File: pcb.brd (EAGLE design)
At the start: 88.9 x 70 mm, 83 parts, among them U1.1 REG101-3_DBV_5, U2.1 TCA6416A_PW_24, U4.1 TLV2242_D_8, U6.1 DCH010505S_EDJ_4, U6.2 ISO7221A_D_8, U6.3 TS5A3357_DCU_8, U6.4 TS5A3357_DCU_8, U8.1 DCH010505S_EDJ_4, U8.2 MAX232E_D_16, U8.3 ISO7221A_D_8, U9.1 DCH010505S_EDJ_4, U9.2 ISO7420Fx

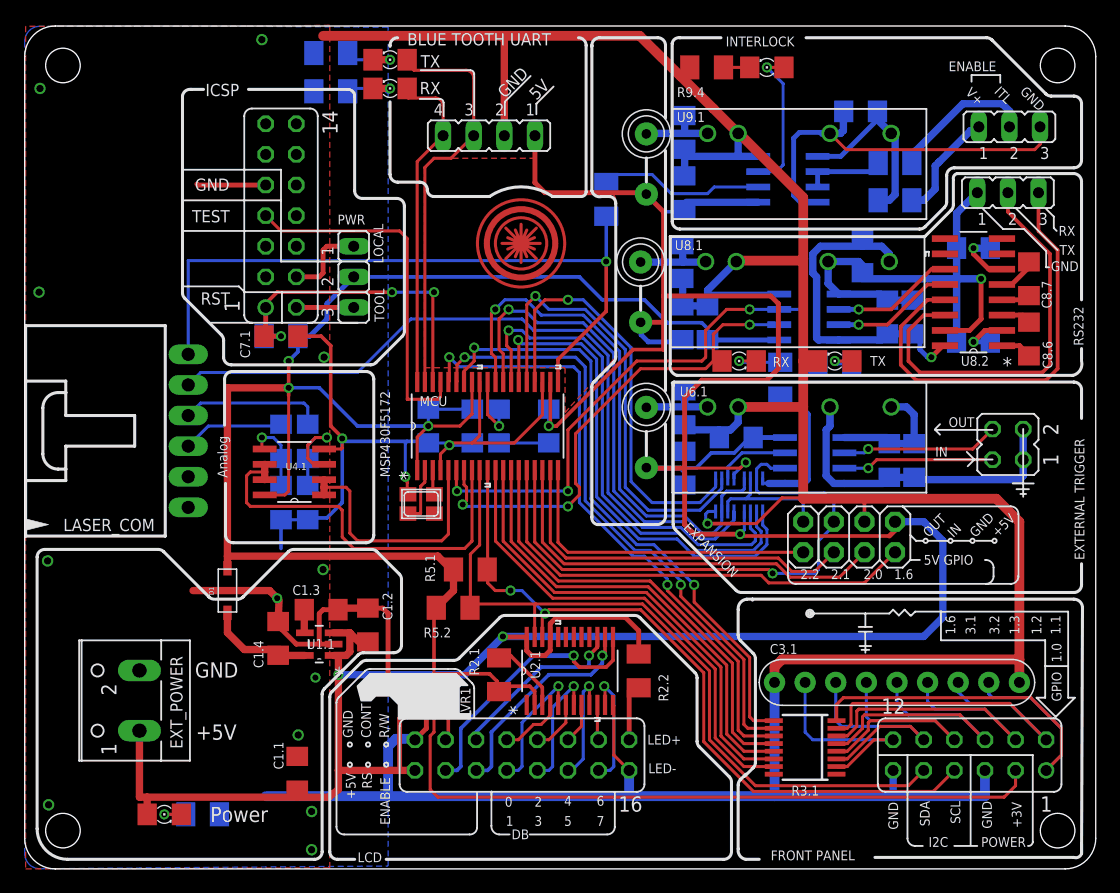
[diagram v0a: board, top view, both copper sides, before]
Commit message: Separated Analog ground from digital ground
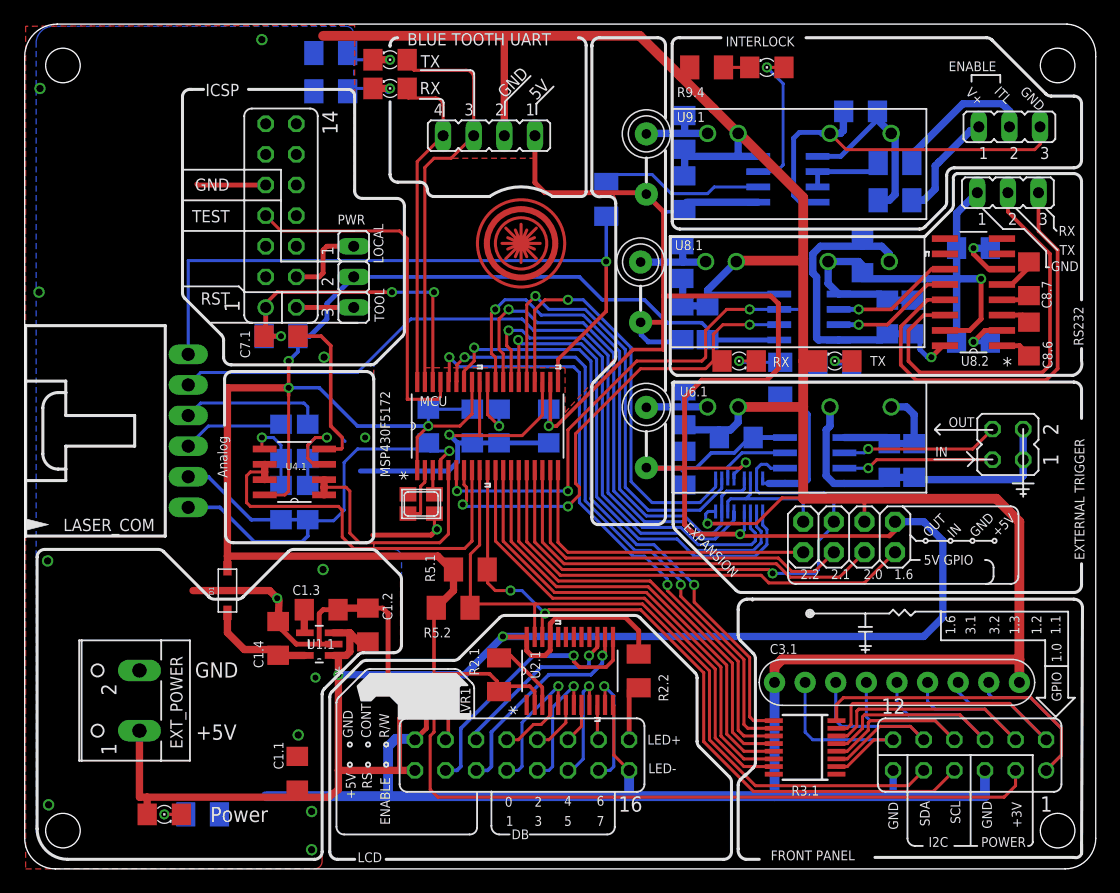
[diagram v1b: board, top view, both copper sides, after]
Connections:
- removed net G2: XTL.2
- new net A_GND: C5.1.2, LASER_COM.1, LASER_COM.2, MCU.4, R4.1.1, R4.3.1
- new net G1: XTL.4
- net GND: now also XTL.2; no longer C5.1.2, LASER_COM.1, LASER_COM.2, MCU.4, R4.1.1, R4.3.1, XTL.4
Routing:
- net A_GND: track 0.00 -> 43.1 mm, vias 0 -> 1
- net GND: track 408.3 -> 395.6 mm
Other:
- board size 88.9 x 70 mm -> 88.9 x 70.1 mm

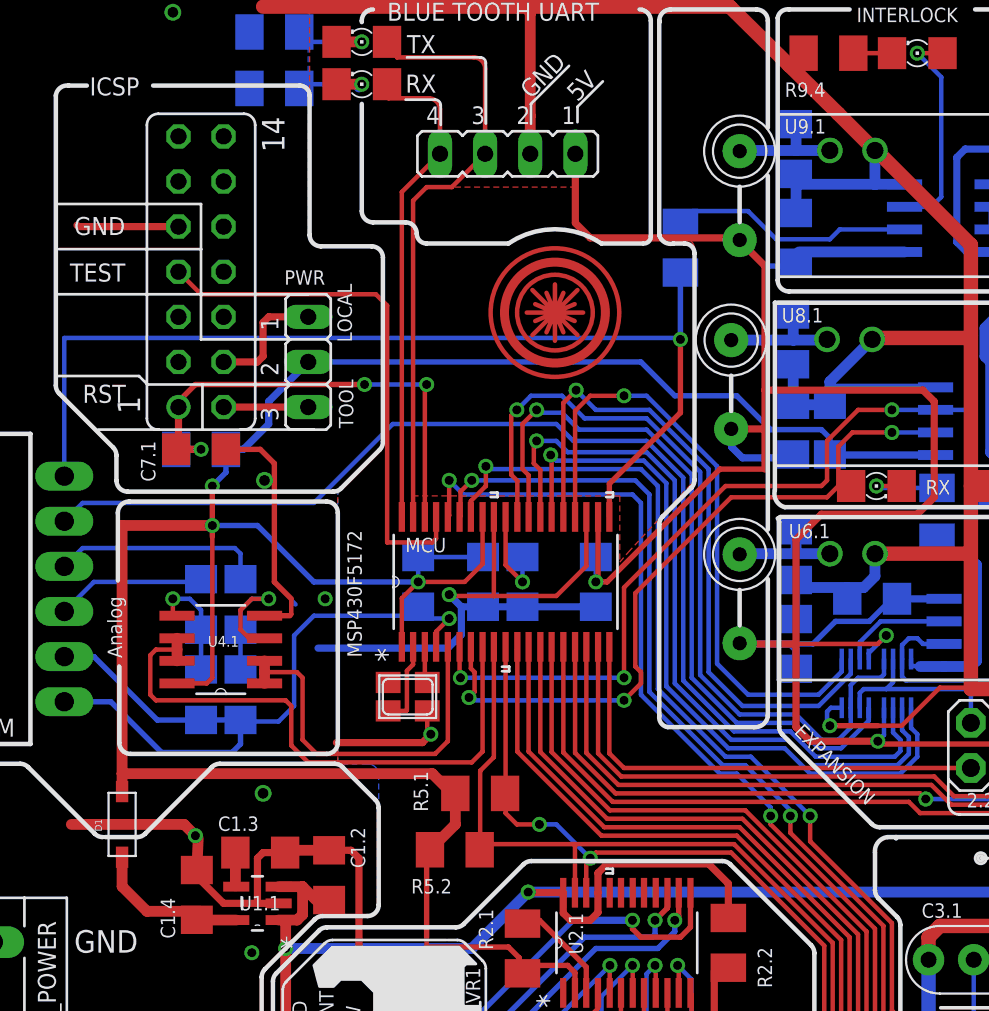
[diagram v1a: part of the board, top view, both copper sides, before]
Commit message: Analog ground isolation
Moved opamp to Agnd
added Agnd plane
Added decoupling cap to opamp
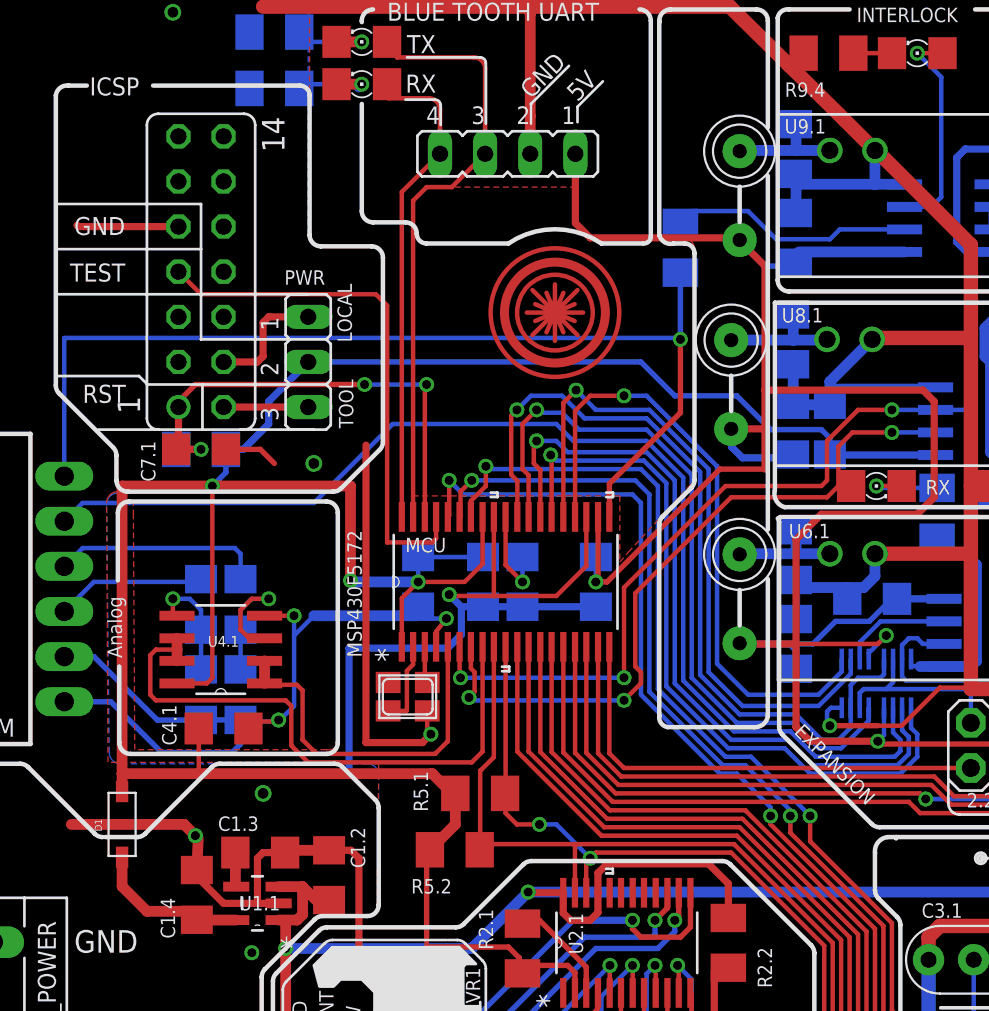
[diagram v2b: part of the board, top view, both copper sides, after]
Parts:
- added C4.1: 10 uF, adafruit:C1206
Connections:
- net A_GND: now also C4.1.1, U4.1.4
- net GND: no longer U4.1.4
- net VCC_3V: now also C4.1.2
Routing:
- net GND: track 395.6 -> 405.8 mm, vias 16 -> 15
- net VCC_3V: track 209.9 -> 218.7 mm
- net A_GND: track 43.1 -> 47.5 mm, vias 1 -> 3
- net LASER_CURRENT_3V: track 21.1 -> 22.5 mm
- net RX1: track 40.4 -> 41.1 mm
- added copper zone on layer 1, net A_GND
- added copper zone on layer 16, net A_GND

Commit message: Updated Schematic.
Updated schematic layout. Added frame, updated passive components, set
(some) resistor values.
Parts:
- removed C1.1, C4.1, C6.3, C8.4: 10 uF, adafruit:C1206
- removed C1.2, C1.4, C5.2, C5.3, C5.4, C6.4, C6.5, C8.10, C8.3, C8.9: 0.1 uF, adafruit:C1206
- removed C1.3: 0.01 uF, adafruit:C1206
- removed C6.1, C8.1, C9.1: 4.7 uF, adafruit:C1206
- removed C6.2, C8.2, C9.2, C9.3: 2.2 uF, adafruit:C1206
- removed C7.1: 2.2 nF, adafruit:C1206
- removed C8.5, C8.6, C8.7, C8.8: 1 uF, adafruit:C1206
- removed D1: (no value), adafruit:SOD-123
- removed L6.1, L8.1, L9.1: 3 uH, adafruit:FB
- removed R1.1, R7.1: 47k, adafruit:M1206
- removed R2.1: 10k, adafruit:M1206
- removed R2.2: (no value), adafruit:M1206
- removed R4.1: 1M, adafruit:R1206
- removed R4.2: 0R, adafruit:R1206
- removed R4.3: 600k, adafruit:R1206
- removed R4.4: 400k, adafruit:R1206
- removed R5.1, R5.2: 43k, adafruit:M1206
- removed R8.1, R8.2, R8.3, R8.4, R9.4: 100k, adafruit:M1206
- removed R9.2: 500k, adafruit:M1206
- removed U4.1: TLV2242_D_8, TI:D8
- added C1, C11, C12, C13, C16, C18, C2, C23, C27, C3, C6, C7, C8: .1uF, rc-master-smd:C0603
- added C10, C17, C26, C5: 10uF, rc-master-smd:C0603
- added C14, C15: 1uF, rc-master-smd:C0603
- added C19, C21, C24: 2.2uF, rc-master-smd:C0603
- added C20, C22, C25: 4.7uF, rc-master-smd:C0603
- added C4: 2.2nF, rc-master-smd:C0603
- added C9: .01uF, rc-master-smd:C0603
- added D2: BAR43, diode:SOT23
- added L1, L2, L3: 3uH, rc-master-smd:L0805
- added R1, R3: 1.2K, rc-master-smd:R0603
- added R10, R11, R12, R13, R6, R9: 330, rc-master-smd:R0603
- added R2: 47K, rc-master-smd:R0603
- added R4: 600K, rc-master-smd:R0603
- added R5: 400K, rc-master-smd:R0603
- added R7: 10K, rc-master-smd:R0603
- added R8: (no value), rc-master-smd:R0603
- added U1: TLV2242_D_8, op-amp:SO08
- C5.1: device adafruit:C1206 -> rc-master-smd:C0603
- R9.3: value 500k -> 1.2K
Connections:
- net TTL_IN_ISO renamed N$11
- removed net G1: XTL.4
- removed net ITL_POWER: C9.2.1, L9.1.P$2, U9.1.1
- removed net N$10: R4.3.2, R4.4.1, U4.1.3
- removed net N$11 (its old number): C6.2.1, L6.1.P$2, U6.1.1
- removed net N$31: LED8.2.C, R8.2.1
- removed net N$35: H9.1.1, R9.2.1
- removed net N$8 (its old number): R4.1.2, R4.2.1, U4.1.5
- removed net SERIAL_GND: C8.3.1, C8.4.1, C8.5.1, C8.8.1, C8.9.2, H8.1.1, U8.1.3, U8.2.15, U8.3.5
- removed net SERIAL_VCC: C8.3.2, C8.4.2, C8.9.1, U8.1.4, U8.2.16, U8.3.8
- removed net VCC_3V: C4.1.2, C5.1.1, C5.2.1, C8.10.1, D1.C, H3.1.3, H7.1.2, MCU.1, MCU.31, R2.1.2, R5.1.1, R5.2.1, R7.1.2, U2.1.2, U4.1.8, U8.3.1
- removed net VCC_3V_SUPPLY: C1.4.1, D1.A, U1.1.5
- new net +3V3: C1.1, C11.1, C16.2, C5.1.1, C6.2, D2.1, H3.1.3, H7.1.2, MCU.1, MCU.31, R1.1, R2.2, R3.1, R7.2, U1.1.5, U1.8, U2.1.2, U8.3.1
- new net +5V: C10.1, C20.1, C22.1, C23.2, C25.1, C27.2, C3.1, C7.1, C8.2, D2.3, EXT_POWER.1, H6.1.8, H8.2.1, L1.2, L2.2, L3.2, LED1.A, MCU.21, R8.2, U1.1.1, U1.1.3, U2.1.21, U2.1.24, U6.2.8, U6.3.8, U6.4.8, U9.2.8, VR1.3
- new net N$18: R4.1, R5.1, U1.3
- new net N$20: LED1.C, R6.2
- new net N$23: LED8.1.C, R9.2
- new net N$32: C24.1, L3.1, U6.1.1
- new net SGND: C12.1, C13.1, C17.2, C18.2, H8.1.1, U8.1.3, U8.2.15, U8.3.5
- new net VBUS: C17.1, C18.1, U8.1.4, U8.2.16, U8.3.8
- net A_GND: no longer C4.1.1, C5.1.2, MCU.4, R4.1.1, R4.3.1, U4.1.4
- net GND: now also C1.2, C10.2, C11.2, C16.1, C19.2, C2.2, C20.2, C21.2, C22.2, C23.1, C24.2, C25.2, C27.1, C3.2, C4.2, C5.1.2, C6.1, C7.2, C8.1, C9.2, MCU.4, R10.1, R11.1, R12.1, R13.2, R4.2, R6.1, R9.1, U1.4, U9.2.5, XTL.4; no longer C1.1.2, C1.2.2, C1.3.2, C1.4.2, C5.2.2, C5.3.2, C5.4.2, C6.1.2, C6.2.2, C6.5.1, C7.1.2, C8.1.2, C8.10.2, C8.2.2, C9.1.2, C9.2.2, LED8.1.C, R1.1.1, R8.2.2, R8.3.1, R8.4.1, R9.4.1, U9.2.8
- net LASER_CURRENT: now also R5.2; no longer R4.4.2
- net LASER_CURRENT_3V: now also U1.1, U1.2; no longer U4.1.1, U4.1.2
- net LASER_TEMPERATURE: now also U1.5; no longer R4.2.2
- net LASER_TEMPERATURE_3V: now also U1.6, U1.7; no longer U4.1.6, U4.1.7
- net N$1: now also C14.1, U8.2.4; no longer C8.6.1, U8.2.1
- net N$13: now also C9.1; no longer C1.3.1
- net N$15: now also R7.1; no longer R2.1.1
- net N$2: now also C14.2, U8.2.5; no longer C8.6.2, U8.2.3
- net N$24: now also C2.1; no longer C5.3.1
- net N$25: now also LED8.2.C, R10.2; no longer LED1.C, R1.1.2
- net N$26: now also LED8.4.C, R11.2; no longer LED8.3.C, R8.3.2
- net N$27: now also C26.2, H9.1.1; no longer C9.3.1, R9.2.2
- net N$28: now also C26.1; no longer C9.3.2
- net N$29: now also LED8.3.C, R12.2; no longer LED8.4.C, R8.4.2
- net N$3: now also C15.1, U8.2.3; no longer C8.7.1, U8.2.4
- net N$30: now also R13.1; no longer R9.4.2
- net N$33: now also C19.1, L1.1, U8.1.1; no longer LED8.1.A, R8.1.2
- net N$4: now also C15.2, U8.2.1; no longer C8.7.2, U8.2.5
- net N$5: now also C13.2; no longer C8.8.2
- net N$6: now also C12.2; no longer C8.5.2
- net N$9: now also C21.1, L2.1, U9.1.1; no longer C8.2.1, L8.1.P$2, U8.1.1
- net RST: now also C4.1, R2.1; no longer C7.1.1, R7.1.1
- net SCL: now also R3.2; no longer R5.1.2
- net SDA: now also R1.2; no longer R5.2.2
- net TTL_GND_ISO: now also C5.1; no longer C6.3.2, C6.4.2
- net TTL_ISO_VCC: now also C5.2; no longer C6.3.1, C6.4.1
- net TX1: now also LED8.1.A; no longer R8.1.1
- net VCC_5V: no longer C1.1.1, C1.2.1, C5.4.1, C6.1.1, C6.5.2, C8.1.1, C9.1.1, EXT_POWER.1, H6.1.8, H8.2.1, L6.1.P$1, L8.1.P$1, L9.1.P$1, LED1.A, MCU.21, R2.2.2, U1.1.1, U1.1.3, U2.1.21, U2.1.24, U6.2.8, U6.3.8, U6.4.8, U9.2.5, VR1.3
- net VCC_LED: now also R8.1; no longer R2.2.1
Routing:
- net VCC_3V: track 218.7 -> 0.00 mm, vias 3 -> 0
- net GND: track 405.8 -> 210.9 mm, vias 15 -> 13
- net VCC_5V: track 275.7 -> 99.5 mm, vias 5 -> 2
- net +5V: track 0.00 -> 95.1 mm, vias 0 -> 3
- net SERIAL_GND: track 43.3 -> 0.00 mm, vias 1 -> 0
- net SERIAL_VCC: track 28.1 -> 0.00 mm, vias 1 -> 0
- net A_GND: track 47.5 -> 20.5 mm, vias 3 -> 0
- net VBUS: track 0.00 -> 24.0 mm, vias 0 -> 1
- net +3V3: track 0.00 -> 13.4 mm
- net N$11: track 12.6 -> 0.00 mm, vias 1 -> 0
- net N$8: track 12.4 -> 0.00 mm, vias 1 -> 0
- net N$14: track 12.2 -> 0.00 mm
- net VCC_3V_SUPPLY: track 9.75 -> 0.00 mm
- net N$10: track 9.70 -> 0.00 mm, vias 1 -> 0
- net N$35: track 9.19 -> 0.00 mm
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
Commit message: Reliability Changes
Changed oscillator circuit, changed voltage regulator to larger package
(current capability), added TVS diodes and current limiting resistors to
I/O. Updated schematic layout.
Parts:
- removed C9: .01uF, rc-master-smd:C0603
- removed U1.1: REG101-3_DBV_5, TI:DBV5@1
- removed XTL: (no value), adafruit:NX3225
- added C28: 10uF, rc-master-smd:C0603
- added C29, C30: 22pF, rc-master-smd:C0603
- added C31: 4.7uF, rc-master-smd:C0603
- added C32: .1uF, rc-master-smd:C0603
- added D1: BAS70, diode:SOT23
- added D3, D4, D5, D6: SRV05-4, diode:SOT23-6L
- added R14, R15, R16, R17, R18, R19, R20, R21: 330, rc-master-smd:R0603
- added U2: LT1117-S, v-reg:SOT223
- added Y1: 16MHZ, crystal:HC49/S
- C2: value .1uF -> .47uF
- D2: value BAR43 -> SRV05-4; device diode:SOT23 -> diode:SOT23-6L
- R9.1: value 100k -> 47K
- moved D2 176.1 mm to (-4.13, -260.3)
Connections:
- removed net A_GND: LASER_COM.1, LASER_COM.2
- removed net VCC_5V: H2.1.2
- new net N$10: LASER_COM.3, R17.2
- new net N$31: LASER_COM.5, R15.2
- new net N$34: LASER_COM.6, R14.2
- new net N$35: R21.1
- new net N$36: R18.1
- new net N$37: R19.1
- new net N$38: R20.1
- net +3V3: now also C28.1, C31.1, C32.2, D1.1, D2.5, D3.5, D5.5, U2.2, U2.4; no longer D2.1, U1.1.5
- net +5V: now also D1.3, D4.5, D6.5, H2.1.2, U2.3; no longer D2.3, U1.1.1, U1.1.3
- net 3VIO-0H: now also D3.1
- net 3VIO-1H: now also D3.3
- net 3VIO-2H: now also D3.4
- net 3VIO-3H: now also D2.6
- net 3VIO-4H: now also D2.1
- net 3VIO-5H: now also D2.3
- net 3VIO-6H: now also D2.4
- net 5VIO-0: now also D4.4, R20.2
- net 5VIO-1: now also D4.3, R19.2
- net 5VIO-2: now also D4.1, R18.2
- net 5VIO-3: now also D4.6, R21.2
- net GND: now also C28.2, C29.2, C30.2, C31.2, C32.1, D2.2, D3.2, D4.2, D5.2, D6.2, LASER_COM.1, LASER_COM.2, U2.1; no longer C9.2, U1.1.2, XTL.2, XTL.4
- net LASER_CURRENT: now also D6.3, R16.1; no longer LASER_COM.4
- net LASER_ILK: now also D6.6, R14.1; no longer LASER_COM.6
- net LASER_TEMPERATURE: now also D6.4, R17.1; no longer LASER_COM.3
- net LASER_TTL: now also D6.1, R15.1; no longer LASER_COM.5
- net N$13: now also LASER_COM.4, R16.2; no longer C9.1, U1.1.4
- net N$21: now also C29.1, Y1.2; no longer XTL.1
- net N$22: now also C30.1, Y1.1; no longer XTL.3
- net SCL: now also D5.4
- net SDA: now also D5.3
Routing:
- net VCC_5V: track 99.5 -> 0.00 mm, vias 2 -> 0
- net A_GND: track 20.5 -> 0.00 mm
- net GND: track 210.9 -> 231.4 mm
- net LASER_CURRENT: track 10.5 -> 0.00 mm
- net LASER_TEMPERATURE: track 8.24 -> 0.00 mm
- net LASER_ILK: track 57.9 -> 50.1 mm
- net +3V3: track 13.4 -> 5.92 mm
- net LASER_TTL: track 66.5 -> 65.1 mm
- net N$21: track 4.78 -> 3.77 mm

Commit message: Connector Update
Added DB25 laser connector and replaced power connector with mini-fit
Jr. Added logic buffer to laser outputs. Minor additional updates.
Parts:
- removed C3.1: 100 nF, TI:SIP9
- removed D6: SRV05-4, diode:SOT23-6L
- removed EXT_POWER: (no value), con-wago-500:W237-102
- removed H7.1: (no value), jumper:JP2
- removed LASER_COM: C-GRID-06-70553, con-molex:70553-06
- removed R14, R15, R16, R17: 330, rc-master-smd:R0603
- added C33, C34, C35, C36, C37, C38, C39, C40, C9: .1uF, rc-master-smd:C0603
- added CN1: NC182M25, custom:NC182M25
- added H9.2: (no value), jumper:JP2
- added P1: 39-30-02?, con-molex-mini-fit:39-30-?02?
- added R22: 330, rc-master-smd:R0603
- added U3, U4: SN74LVC1G17DBV, 74LV:SOT23-5
- R8: value (none) -> 0
- U9.2: value ISO7420Fx -> ISO7220D
- moved U2 308.5 mm to (19.3, 15.3)
- moved C28 229.6 mm to (17.5, 6.38)
- moved R6 100.9 mm to (15.4, 4.38), turned to 180 degrees
- moved C11 91.1 mm to (17.9, 8.87)
- moved C10 87.3 mm to (14.8, 10.1), turned to 90 degrees
- moved C7 78.6 mm to (14.9, 14.2), turned to 90 degrees
- moved LED8.1 0.63 mm to (67.9, 42.1)
- moved R3.1 0.51 mm to (64.3, 10.1)
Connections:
- net VCC_LED renamed N$41
- removed net N$17: H7.1.3, JP4.2
- removed net N$31: LASER_COM.5, R15.2
- removed net N$34: LASER_COM.6, R14.2
- removed net N$35: R21.1
- removed net N$36: R18.1
- removed net N$37: R19.1
- removed net N$38: R20.1
- new net 5VIO-4: D4.4, R20.1
- new net N$12: CN1.1, U3.4
- new net N$39: R22.2, VR1.3
- net +3V3: now also H9.2.2; no longer H7.1.2
- net +5V: now also C39.1, C40.1, CN1.10, CN1.11, CN1.12, CN1.13, CN1.5, CN1.6, CN1.7, CN1.8, CN1.9, P1.2, R22.1, U3.5, U4.5; no longer D6.5, EXT_POWER.1, VR1.3
- net 3VIO-0H: now also C9.1; no longer C3.1.1
- net 3VIO-1H: now also C33.1; no longer C3.1.2
- net 3VIO-2H: now also C34.1; no longer C3.1.3
- net 3VIO-3H: now also C35.1; no longer C3.1.4
- net 3VIO-4H: now also C36.1; no longer C3.1.5
- net 3VIO-5H: now also C37.1; no longer C3.1.6
- net 3VIO-6H: now also C38.1; no longer C3.1.7
- net 5VIO-0: no longer D4.4
- net 5VIO-1: now also D4.6, R21.1; no longer D4.3
- net 5VIO-2: now also R18.1
- net 5VIO-3: now also D4.3, R19.1; no longer D4.6
- net GND: now also C33.2, C34.2, C35.2, C36.2, C37.2, C38.2, C39.2, C40.2, C9.2, CN1.17, CN1.18, CN1.19, CN1.20, CN1.21, CN1.22, CN1.23, CN1.24, CN1.25, CN1.G1, CN1.G2, P1.1, U3.3, U4.3; no longer C3.1.BUS, C3.1.BUS2, D6.2, EXT_POWER.2, LASER_COM.1, LASER_COM.2
- net LASER_CURRENT: now also CN1.2; no longer D6.3, R16.1
- net LASER_ILK: now also U3.2; no longer D6.6, R14.1
- net LASER_TEMPERATURE: now also CN1.3; no longer D6.4, R17.1
- net LASER_TTL: now also U4.2; no longer D6.1, R15.1
- net N$10: now also CN1.14, U4.4; no longer LASER_COM.3, R17.2
- net N$13: now also H9.2.1, JP4.4; no longer LASER_COM.4, R16.2
- net N$16: now also H9.2.3, JP4.2; no longer H7.1.1, JP4.4
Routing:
- net GND: track 231.4 -> 123.1 mm, vias 13 -> 3
- net 3VIO-0H: track 37.5 -> 25.3 mm
- net LASER_TEMPERATURE_3V: track 31.6 -> 20.0 mm
- net 3VIO-6H: track 17.3 -> 6.13 mm
- net 3VIO-4H: track 22.8 -> 12.0 mm
- net 3VIO-5H: track 20.0 -> 9.33 mm
- net 3VIO-2H: track 27.8 -> 17.5 mm
- net 3VIO-3H: track 25.0 -> 14.8 mm
- net 3VIO-1H: track 30.2 -> 20.2 mm
- net +5V: track 95.1 -> 86.1 mm
- net N$16: track 5.03 -> 0.00 mm
- net N$17: track 4.76 -> 0.00 mm
- net N$41: track 4.73 -> 0.00 mm
- net LASER_TTL: track 65.1 -> 63.9 mm
- net 3VIO-1: track 39.2 -> 38.7 mm
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- removed copper zone on layer 1, net A_GND
- removed copper zone on layer 16, net A_GND
- removed copper zone on layer 1, net GND
- removed copper zone on layer 16, net GND
- removed copper zone on layer 1, net N$12
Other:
- outline, holes or cut-outs redrawn
- board text removed: "Current"
- board text removed: "Interlock"
- board text removed: "Temperature"
- board text removed: "Trigger"
